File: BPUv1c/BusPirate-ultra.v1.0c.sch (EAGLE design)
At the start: 169 parts, among them CON1 USB-C-12, IC1 SN74LVC1T45DBV, IC10 23LC1024, IC11 74HCT4051, IC12 MCP1824_ADJ, IC2 SN74LVC1T45DBV, IC3 SN74LVC1T45DBV, IC4 SN74LVC1T45DBV, IC5 SN74LVC1T45DBV, IC6 SN74LVC1T45DBV, IC7 SN74LVC1T45DBV, IC8 SN74LVC1T45DBV, IC9 23LC1024, J1 CON_HEADER_1X04, J2 CON_HEADER_1X10-RIGHT_ANGLED_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, J3 CON_MOLEX_MALE_SMT_SH_1.25, Q1 DMMT3906W, Q2 PMV65XP, U1 74LVC1G07DBV, U10 74HCT4066PW, U11 74HCT4066PW, U12 W25X40CL, U13 74LVC245A, U14 MCP6001, U15 MCP6001, U16 ICE40HX4K, U2 74LVC1G07DBV, U3 74LVC1G07DBV, U4 74LVC1G07DBV, U5 STM32F103ZX, U6 74LVC1G07DBV, U7 74LVC1G07DBV, U8 74LVC1G07DBV, U9 74LVC1G07DBV

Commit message: new BPUltra.v.1.0C revision removed some text labels renamed BPIO pin labels fix bom parts naming change back to original SC-70-5 and SC-70-6 footprints for 74LVC1G07DBV and SN74LVC1T45DBV added decoupling caps for open drain buffers broke RN3 to individual 10K R603 resistors Added 1uF 0603 cap to U14 connect OE (pin 80) and DIR (pin 81) of latch (245) to FPGA Change values of the following parts: R27 to 100K R32 to 10K R31 to 99.22K R30 to 77.96K R26 to 0R R36 to 0R R33 to 0R R34 to 65K R35 to 100K C24 to DNP C23 to 4.7uF C29 to 4.7uF D1 to 1N4148 Q2 to PMV65XP
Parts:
- added C66, C67, C68, C69, C70, C71, C72: 0.1uF, dp_devices.v6:CAPACITOR_NPOL-0402
- added C73: 0.1uF, dp_devices.v6:CAPACITOR_NPOL-0603
- C1, C5: device rcl:C-EUC0402 -> dp_devices.v6:CAPACITOR_NPOL-0402
- C10, C11, C12, C13, C14, C15, C16, C2, C3, C4, C6, C7, C8, C9: device resistor:C-EUC0402 -> dp_devices.v6:CAPACITOR_NPOL-0402
- C17, C18, C20, C21, C22, C24, C25, C26, C27, C30, C31, C33, C34, C35, C37, C38, C40, C41, C42, C43, C44, C45, C46, C47, C48, C49, C50, C51, C52, C53, C54, C55, C56, C57, C58, C60, C61, C62, C63: device rcl:C-EUC0603 -> dp_devices.v6:CAPACITOR_NPOL-0603
- C19, C64: device rcl:CPOL-EUSMCA -> dp_devices.v6:CAPACITOR_POL-SMC_A
- C28, C39: value 1uf -> 1uF; device rcl:C-EUC0603 -> dp_devices.v6:CAPACITOR_NPOL-0603
- C65: value 1uF -> 0.1uF; device dp_devices.v6:CAPACITOR_NPOL-0603 -> dp_devices.v6:CAPACITOR_NPOL-0402
- IC1, IC2, IC3, IC4, IC5, IC6, IC7, IC8: device dp_devices.v6:IC_BUFF_SN74LVC1T45DBV-EXTENDED -> dp_devices.v6:IC_BUFF_SN74LVC1T45DBV-SC-70-6
- R1, R10, R11, R12, R13, R14, R15, R16, R17, R18, R19, R2, R20, R21, R22, R23, R24, R3, R4, R5, R6, R7, R8, R9: device resistor:R-EU_R0402 -> dp_devices.v6:RESISTOR-0402
- R26, R29, R37, R38, R41, R42, R43, R44, R45: device rcl:R-EU_R0603 -> dp_devices.v6:RESISTOR-0603
- R33, R36, R39, R40: device resistor:R-EU_R0603 -> dp_devices.v6:RESISTOR-0603
- R46, R47, R48, R49: device dp_devices:RESISTOR-0603 -> dp_devices.v6:RESISTOR-0603
- U1, U2, U3, U4, U6, U7, U8, U9: device dp_devices.v6:IC_BUFF_74LVC1G07-EXTENDED -> dp_devices.v6:IC_BUFF_74LVC1G07
- U15: device dp_devices.v6:IC_MCP6001 -> dp_devices.v6:IC_OP-AMP_MCP6001
- XTAL1: device dp_devices:OSC-XTAL-12M -> dp_devices.v6:OSC-XTAL-12M
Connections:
- net 1V2: now also C31.1, C35.1, C39.2, C43.1, C54.1, C55.1; no longer C31.2, C35.2, C39.1, C43.2, C54.2, C55.2
- net 3V3: now also C1.2, C10.2, C11.2, C12.2, C17.1, C2.2, C21.1, C22.1, C25.1, C28.2, C3.2, C30.1, C33.1, C34.1, C4.2, C42.1, C44.1, C45.1, C46.1, C47.1, C48.1, C49.1, C50.1, C51.1, C52.1, C53.2, C56.1, C57.1, C58.2, C60.1, C61.2, C62.1, C63.1, C65.2, C66.2, C67.2, C68.2, C69.2, C70.2, C71.2, C72.2, C9.2; no longer C1.1, C10.1, C11.1, C12.1, C17.2, C2.1, C21.2, C22.2, C25.2, C28.1, C3.1, C30.2, C33.2, C34.2, C4.1, C42.2, C44.2, C45.2, C46.2, C47.2, C48.2, C49.2, C50.2, C51.2, C52.2, C53.1, C56.2, C57.2, C58.1, C60.2, C61.1, C62.2, C63.2, C9.1
- net ADC1: now also R52.1; no longer R52.2
- net GND: now also C1.1, C10.1, C11.1, C12.1, C13.2, C14.2, C15.2, C16.2, C17.2, C18.2, C2.1, C20.2, C21.2, C22.2, C24.1, C25.2, C26.1, C27.1, C28.1, C3.1, C30.2, C31.2, C33.2, C34.2, C35.2, C39.1, C4.1, C40.1, C41.1, C42.2, C43.2, C44.2, C45.2, C46.2, C47.2, C48.2, C49.2, C5.2, C50.2, C51.2, C52.2, C53.1, C54.2, C55.2, C56.2, C57.2, C58.1, C6.2, C60.2, C61.1, C62.2, C63.2, C65.1, C66.1, C67.1, C68.1, C69.1, C7.2, C70.1, C71.1, C72.1, C73.1, C8.2, C9.1, R50.2, R52.2; no longer C1.2, C10.2, C11.2, C12.2, C13.1, C14.1, C15.1, C16.1, C17.1, C18.1, C2.2, C20.1, C21.1, C22.1, C24.2, C25.1, C26.2, C27.2, C28.2, C3.2, C30.1, C31.1, C33.1, C34.1, C35.1, C39.2, C4.2, C40.2, C41.2, C42.1, C43.1, C44.1, C45.1, C46.1, C47.1, C48.1, C49.1, C5.1, C50.1, C51.1, C52.1, C53.2, C54.1, C55.1, C56.1, C57.1, C58.2, C6.1, C60.1, C61.2, C62.1, C63.1, C65.2, C7.1, C8.1, C9.2, R51.2, R53.1
- net MCU_ADC6: now also R50.1, R51.2; no longer R50.2, R51.1
- net N$21: now also R53.1; no longer R52.1
- net N$31: now also C24.2; no longer C24.1
- net N$8: now also C20.1; no longer C20.2
- net N$9: now also C18.1; no longer C18.2
- net VREF/VOUT: now also C13.1, C14.1, C15.1, C16.1, C5.1, C6.1, C7.1, C8.1, R51.1; no longer C13.2, C14.2, C15.2, C16.2, C5.2, C6.2, C7.2, C8.2, R50.1
- net VUSB: now also C26.2, C27.2, C40.2, C41.2, C73.2; no longer C26.1, C27.1, C40.1, C41.1, C65.1
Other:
- note removed: "TODO: change SC70 footprint to proper SC70 Fix part numbering, part naming change VR1 to MCP1700-33 SOT-89 add 4.7uF on its input and 1uF on the output VR2 also to MCP1700-12, same caps added"
- moved on the sheet: C59, C65, R50, R51, R52, R53, U1P, U2P, U4P, U6P, U7P, U8P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

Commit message: re-number parts logically changed C302 to 1uF add 4.7uF input cap on VR1 add 4.7uF input cap on VR2 add RC filter 25R and 1.5nF on ADC MUX buffer
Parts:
- removed C27, C37: 0.1uF, dp_devices.v6:CAPACITOR_NPOL-0603
- removed C38: 1uF, dp_devices.v6:CAPACITOR_NPOL-0603
- removed CON1: USB-C-12, usbc:USB-C-12
- removed D1: 1N4148, dp_devices.v6:DIODE-SOD-123
- removed IC11: 74HCT4051, dp_devices.v6:IC_74HCT4051
- removed R33, R36: 0R, dp_devices.v6:RESISTOR-0603
- removed R52, R53: 10K, dp_devices.v6:RESISTOR-0603
- removed RN1, RN2: 2K, dp_devices:RNETWORK
- removed U15: MCP6001, dp_devices.v6:IC_OP-AMP_MCP6001
- added C200, C201: 0.1uF, dp_devices.v6:CAPACITOR_NPOL-0603
- added C202: 1uF, dp_devices.v6:CAPACITOR_NPOL-0603
- added C203: 1.5nF, dp_devices.v6:CAPACITOR_NPOL-0603
- added C305, C307: 4.7uF, dp_devices.v6:CAPACITOR_NPOL-0603
- added D200: 1N4148, dp_devices.v6:DIODE-SOD-123
- added J4: CON_MOLEX_MALE_SMT_SH_1.25, dp_devices.v6:CON_MOLEX_MALE_SMT_SH_1.25
- added R200, R201: 0R, dp_devices.v6:RESISTOR-0603
- added R202, R204: 10K, dp_devices.v6:RESISTOR-0603
- added R203: 25R, dp_devices.v6:RESISTOR-0603
- added RN500, RN501: 2K, dp_devices:RNETWORK
- added U200: 74HCT4051, dp_devices.v6:IC_74HCT4051
- added U201: MCP6001, dp_devices.v6:IC_OP-AMP_MCP6001
- C302: value 0.1uF -> 1uF
- J1: value CON_HEADER_1X04 -> USB-C-12; device dp_devices.v6:CON_HEADER_1X04 -> usbc:USB-C-12
- J2: value CON_HEADER_1X10-RIGHT_ANGLED_PTH_SHROUDED -> CON_HEADER_1X04; device dp_devices.v6:CON_HEADER_1X10-RIGHT_ANGLED_PTH_SHROUDED -> dp_devices.v6:CON_HEADER_1X04
- J3: value CON_MOLEX_MALE_SMT_SH_1.25 -> CON_HEADER_1X10-RIGHT_ANGLED_PTH_SHROUDED; device dp_devices.v6:CON_MOLEX_MALE_SMT_SH_1.25 -> dp_devices.v6:CON_HEADER_1X10-RIGHT_ANGLED_PTH_SHROUDED
- renumbered C1 to C400, C10 to C406, C11 to C410, C12 to C414, C13 to C403, C14 to C407, C15 to C411, C16 to C415, C17 to C103, C18 to C100, C19 to C104, C2 to C404, C20 to C101, C21 to C102, C22 to C105, C23 to C300, C24 to C304, C25 to C715, C26 to C303, C28 to C306, C29 to C301, C3 to C408, C30 to C700, C31 to C706, C32 to C708, C33 to C701, C34 to C709, C35 to C702, C36 to C710, C39 to C308, C4 to C412, C40 to C500, C41 to C501, C42 to C106, C43 to C714, C44 to C107, C45 to C707, C46 to C108, C47 to C703, C48 to C711, C49 to C109, C5 to C401, C50 to C704, C51 to C712, C52 to C110, C53 to C600, C54 to C705, C55 to C713, C56 to C111, C57 to C112, C58 to C601, C59 to C113, C6 to C405, C60 to C114, C61 to C602, C62 to C115, C63 to C116, C64 to C800, C65 to C416, C66 to C417, C67 to C418, C68 to C419, C69 to C420, C7 to C409, C70 to C421, C71 to C422, C72 to C423, C73 to C302, C8 to C413, C9 to C402, IC1 to U400, IC10 to U601, IC12 to U300, IC2 to U404, IC3 to U408, IC4 to U412, IC5 to U401, IC6 to U405, IC7 to U409, IC8 to U413, IC9 to U600, L1 to L800, LED1 to LED904, LED2 to LED900, LED3 to LED901, LED4 to LED905, LED5 to LED902, LED6 to LED906, LED7 to LED903, LED8 to LED907, Q1 to Q301, Q2 to Q300, R1 to R402, R10 to R416, R11 to R418, R12 to R422, R13 to R403, R14 to R409, R15 to R415, R16 to R421, R17 to R401, R18 to R405, R19 to R407, R2 to R408, R20 to R411, R21 to R413, R22 to R417, R23 to R419, R24 to R423, R25 to R100, R26 to R306, R27 to R301, R28 to R309, R29 to R702, R3 to R414, R30 to R307, R31 to R300, R32 to R308, R34 to R303, R35 to R304, R37 to R700, R38 to R701, R39 to R805, R4 to R420, R40 to R806, R41 to R800, R42 to R801, R43 to R802, R44 to R803, R45 to R804, R46 to R900, R47 to R901, R48 to R902, R49 to R903, R5 to R400, R50 to R305, R51 to R302, R6 to R404, R7 to R406, R8 to R410, R9 to R412, U1 to U402, U10 to U500, U11 to U501, U12 to U101, U13 to U602, U14 to U301, U16 to U700, U2 to U406, U3 to U410, U4 to U414, U5 to U100, U6 to U403, U7 to U407, U8 to U411, U9 to U415, VR1 to U302, VR2 to U303, XTAL1 to XTAL100
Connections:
- new net N$24: R202.2, R203.1, R204.1
- net 3V3: now also J2.1, J4.9; no longer J1.1, J3.9
- net ADC1: now also C203.1, R203.2; no longer R52.1, R53.2
- net ADC_MUX_EN: now also U200.!E; no longer IC11.!E
- net ADC_MUX_S0: now also U200.S0; no longer IC11.S0
- net ADC_MUX_S1: now also U200.S1; no longer IC11.S1
- net ADC_MUX_S2: now also U200.S2; no longer IC11.S2
- net BPIO0: now also J3.1, RN500A.1, U200.Y0; no longer IC11.Y0, J2.1, RN1A.1
- net BPIO1: now also J3.2, RN500B.1, U200.Y1; no longer IC11.Y1, J2.2, RN1B.1
- net BPIO2: now also J3.3, RN500C.1, U200.Y2; no longer IC11.Y2, J2.3, RN1C.1
- net BPIO3: now also J3.4, RN500D.1, U200.Y3; no longer IC11.Y3, J2.4, RN1D.1
- net BPIO4: now also J3.5, RN501D.2, U200.Y4; no longer IC11.Y4, J2.5, RN2D.2
- net BPIO5: now also J3.6, RN501C.2, U200.Y5; no longer IC11.Y5, J2.6, RN2C.2
- net BPIO6: now also J3.7, RN501B.2, U200.Y6; no longer IC11.Y6, J2.7, RN2B.2
- net BPIO7: now also J3.8, RN501A.2, U200.Y7; no longer IC11.Y7, J2.8, RN2A.2
- net D+: now also J1.DP1, J1.DP2; no longer CON1.DP1, CON1.DP2
- net D-: now also J1.DN1, J1.DN2; no longer CON1.DN1, CON1.DN2
- net DISPLAY_AUX1: now also J4.5; no longer J3.5
- net DISPLAY_AUX2: now also J4.4; no longer J3.4
- net DISPLAY_CS: now also J4.1; no longer J3.1
- net DISPLAY_D/P: now also J4.2; no longer J3.2
- net DISPLAY_PWM: now also J4.3; no longer J3.3
- net DISPLAY_SPI_CLOCK: now also J4.8; no longer J3.8
- net DISPLAY_SPI_MISO: now also J4.7; no longer J3.7
- net DISPLAY_SPI_MOSI: now also J4.6; no longer J3.6
- net GND: now also C200.1, C201.2, C202.2, C203.2, C305.1, C307.1, J1.CHASSIS, J1.GND, J2.2, J4.10, R204.2, U200.GND, U200.VEE, U201.V-; no longer C27.1, C37.2, C38.2, CON1.CHASSIS, CON1.GND, IC11.GND, IC11.VEE, J1.2, J2.10, R52.2, U15.V-
- net N$1: now also J1.VBUS; no longer CON1.VBUS
- net N$14: now also J1.CC1; no longer CON1.CC1
- net N$2: now also RN500B.2; no longer RN1B.2
- net N$20: now also J1.CC2; no longer CON1.CC2
- net N$21: now also R201.2, R202.1; no longer R36.2, R53.1
- net N$3: now also RN500A.2; no longer RN1A.2
- net N$32: now also D200.A, R200.2, U201.+; no longer D1.A, R33.2, U15.+
- net N$33: now also RN501C.1; no longer RN2C.1
- net N$4: now also RN500D.2; no longer RN1D.2
- net N$42: now also RN501D.1; no longer RN2D.1
- net N$44: now also RN501A.1; no longer RN2A.1
- net N$45: now also RN501B.1; no longer RN2B.1
- net N$5: now also RN500C.2; no longer RN1C.2
- net N$61: now also R200.1, U200.Z; no longer IC11.Z, R33.1
- net N$64: now also R201.1, U201.-, U201.OUT; no longer R36.1, U15.-, U15.OUT
- net SWCLK: now also J2.4; no longer J1.4
- net SWDIO: now also J2.3; no longer J1.3
- net VREF/VOUT: now also J3.9; no longer J2.9
- net VUSB: now also C200.2, C201.1, C202.1, C305.2, C307.2, D200.C, U200.VCC, U201.V+; no longer C27.2, C37.1, C38.1, D1.C, IC11.VCC, U15.V+
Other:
- note added: "LATCH"
- note added: "Section 1"
- note added: "Section 2"
- note added: "Section 3"
- note added: "Section 4"
- note added: "Section 5"
- note added: "Section 6"
- note added: "Section 7"
- note added: "Section 8"
- note added: "Section 9"
- moved on the sheet: J3

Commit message: added ADC ADS7041 and wired to FPGA pin 45, 47 and 48 changed 3.3V regulator to bigger MCP1700 changed mux to 16-bit version 74HCT4067, added one new address line S3 to FPGA (not connected yet) connected 1.2V VREG output to MCU ADC pin 35 PA1 changed VUSB voltage divider resistors R805 and R806 to 50K
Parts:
- added C204, C205: 1uF, dp_devices.v6:CAPACITOR_NPOL-0603
- added U202: ADS7041, dp_devices.v6:IC_ADC_ADS7041
- R805, R806: value 10K -> 50K
- U200: value 74HCT4051 -> 74HCT4067; device dp_devices.v6:IC_74HCT4051 -> dp_devices.v6:IC_74HCT4067
- U302: value MCP1801T-3302I/OT -> MCP1700; device dp_devices:MIC5205 -> dp_devices.v6:IC_MCP1700
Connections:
- removed net ADC1: C203.1, R203.2, U100U.ADC12_IN9/TIM3_CH4('00'OR'10')/TIM8_CH3N/TIM1_CH3N('01')/PB1
- removed net N$10: U100U.PA1/USART2_RTS('0')/ADC123_IN1/TIM5_CH2/TIM2_CH2('00')
- removed net N$61: R200.1, U200.Z
- new net ADC_CLOCK: U202.SCLK, U700BANK2.IOB_79
- new net ADC_CS: U202.CS, U700BANK2.IOB_73
- new net ADC_DATA: U202.SDO, U700BANK2.IOB_80
- new net ADC_MUX_S3: U200U.S3
- new net N$46: C203.1, R203.2, U202.AINP
- new net N$47: R200.1, U200U.Z
- net 1V2: now also U100U.PA1/USART2_RTS('0')/ADC123_IN1/TIM5_CH2/TIM2_CH2('00')
- net 3V3: now also U302.VOUT; no longer U302.OUT
- net ADC_MUX_EN: now also U200U.!E; no longer U200.!E
- net ADC_MUX_S0: now also U200U.S0; no longer U200.S0
- net ADC_MUX_S1: now also U200U.S1; no longer U200.S1
- net ADC_MUX_S2: now also U200U.S2; no longer U200.S2
- net BPIO0: now also U200U.Y0; no longer U200.Y0
- net BPIO1: now also U200U.Y1; no longer U200.Y1
- net BPIO2: now also U200U.Y2; no longer U200.Y2
- net BPIO3: now also U200U.Y3; no longer U200.Y3
- net BPIO4: now also U200U.Y4; no longer U200.Y4
- net BPIO5: now also U200U.Y5; no longer U200.Y5
- net BPIO6: now also U200U.Y6; no longer U200.Y6
- net BPIO7: now also U200U.Y7; no longer U200.Y7
- net GND: now also C204.2, C205.2, U200SUP.GND, U202.AINM, U202.GND; no longer U200.GND, U200.VEE
- net VREF/VOUT: now also U200U.Y8
- net VUSB: now also C204.1, C205.1, U200SUP.V+, U202.AVDD, U202.DVDD, U302.VIN; no longer U200.VCC, U302.EN, U302.IN
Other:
- note added: "ADC for 1.2V"
- note added: "Need to connect ADC_MUX_S3 to FPGA"
- note added: "Not sure about this? Powering from VUSB, while STM32 is 3.3V"
- moved on the sheet: C100, C101, C102, C103, C104, C105, C200, C201, C202, C203, C305, C306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

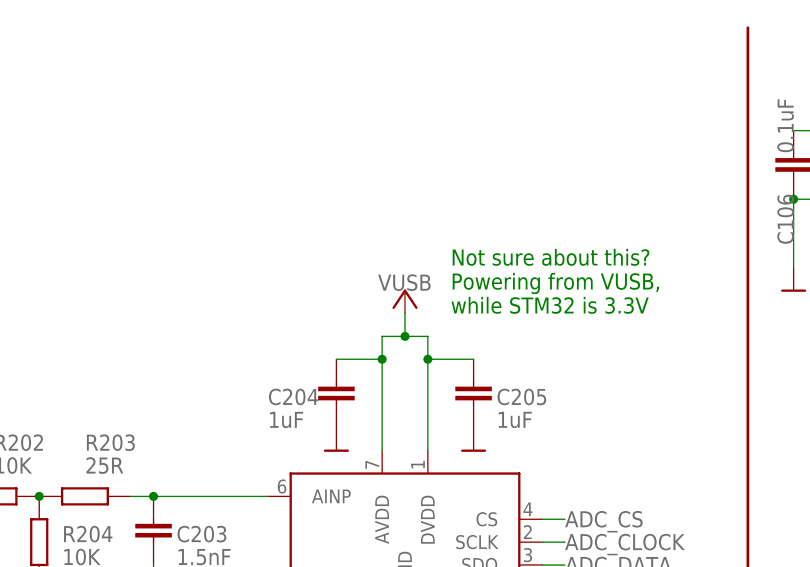
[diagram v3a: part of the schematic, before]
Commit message: change supply of ADC chip to 3.3V
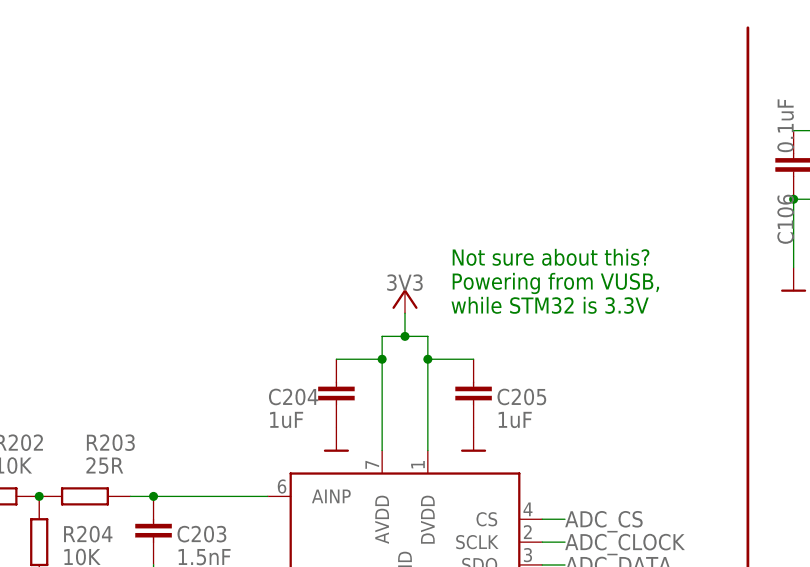
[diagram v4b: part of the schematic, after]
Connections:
- net 3V3: now also C204.1, C205.1, U202.AVDD, U202.DVDD
- net VUSB: no longer C204.1, C205.1, U202.AVDD, U202.DVDD
